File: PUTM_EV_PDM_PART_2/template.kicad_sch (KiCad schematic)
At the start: 4 parts, among them J1 CONN IN, J3 Conn_02x18_Counter_Clockwise, J4 WIRE OUT, J5 Conn_01x37

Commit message: Add files via upload
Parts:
- removed J4: WIRE OUT, Connector_Wire:SolderWire-0.75sqmm_1x02_P4.8mm_D1.25mm_OD2.3mm_Relief, symbol Connector:Conn_01x02_Pin
- removed J5: Conn_01x37, 3RD_party:37 PIN DEUTSCH, symbol Connector_Generic:Conn_01x37
- added J2, J7: UPS-08-07.0-01-L-V, UPS0807001LV, symbol UPS-08-07.0-01-L-V:UPS-08-07.0-01-L-V
- added J4: Conn_01x06_Pin, Connector_IDC:IDC-Header_2x03_P2.54mm_Vertical, symbol Connector:Conn_01x06_Pin
- added J6: +24V OUT, UPT-02-01-01-L-V:SAMTEC_UPT-02-03.0-XX-X-V, symbol Connector:Conn_01x02_Pin
- J1: value CONN IN -> +24V IN; footprint (none) -> DPT13-4P:TE_DTP13-4P
- J3: footprint Connector_IDC:IDC-Header_2x20-1MP_P2.54mm_Latch6.5mm_Vertical -> 3RD_party:37 PIN DEUTSCH
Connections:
- net DASH 24VDC is gone; now on net BRAKE BALANCE 24VDC: J3.15 (Pin_15)
- net DIAGPORT 24VDC is gone; now on net AIR PRESSURE 24VDC: J3.21 (Pin_21)
- net FRONT BOX 24VDC is gone; now on net BRAKE BALANCE 24VDC: J3.28 (Pin_28)
- net HV LOGIKA 2 24VDC is gone; now on net HV LOGIKA 1 24VDC: J3.33 (Pin_33)
- net INVERTER 2 24VDC is gone; now on net INVERTER 1 24VDC: J3.30 (Pin_30)
- net IR CAMS FRONT 24VDC is gone; now on net AIR PRESSURE 24VDC: J3.6 (Pin_6)
- net IR CAMS REAR 24VDC is gone; now on net AIR PRESSURE 24VDC: J3.22 (Pin_22)
- net ODRIVE 3 24VDC is gone; now on net ODRIVE 2 24VDC: J3.24 (Pin_24)
- net ODRIVE 5 24VDC is gone; now on net ODRIVE 4 24VDC: J3.26 (Pin_26)
- net PC 24VDC 2 is gone; now on net PC 24VDC 1: J3.27 (Pin_27)
- net PC 24VDC 4 is gone; now on net PC 24VDC 3: J3.17 (Pin_17)
- net REARBOX 2 24VDC is gone; now on net REARBOX 1 24VDC: J3.3 (Pin_3)
- net REARBOX 4 24VDC is gone; now on net REARBOX 3 24VDC: J3.8 (Pin_8)
- net SDC SOURCE is gone; now on net ASMS SOURCE: J3.9 (Pin_9)
- net TSAL LIGHT 24VDC is gone; now on net BSPD 24VDC: J3.20 (Pin_20)
- net TSAL LOGIC 24VDC is gone; now on net BSPD 24VDC: J3.19 (Pin_19)
- net +24V: now also J6.1 (Pin_1)
- net AIR PRESSURE 24VDC: now also J7.D1, J7.D2, J7.D3, J7.D4, J7.D5, J7.D6
- net ASMS IN: now also J4.3 (Pin_3)
- net ASMS SOURCE: now also J2.C1, J2.C2, J2.C3, J2.C4, J2.C5, J2.C6
- net BRAKE BALANCE 24VDC: now also J2.F1, J2.F2, J2.F3, J2.F4, J2.F5, J2.F6
- net BSPD 24VDC: now also J7.H1, J7.H2, J7.H3, J7.H4, J7.H5, J7.H6
- net CAN_H: now also J4.2 (Pin_2)
- net CAN_L: now also J4.1 (Pin_1)
- net GND: now also J6.2 (Pin_2)
- net GND PDM: now also J4.4 (Pin_4), J4.5 (Pin_5), J4.6 (Pin_6), J7.A1, J7.A2, J7.A3, J7.A4, J7.A5, J7.A6
- net HV LOGIKA 1 24VDC: now also J2.A1, J2.A2, J2.A3, J2.A4, J2.A5, J2.A6
- net INVERTER 1 24VDC: now also J2.G1, J2.G2, J2.G3, J2.G4, J2.G5, J2.G6
- net ODRIVE 1 24VDC: now also J2.D1, J2.D2, J2.D3, J2.D4, J2.D5, J2.D6
- net ODRIVE 2 24VDC: now also J7.F1, J7.F2, J7.F3, J7.F4, J7.F5, J7.F6
- net ODRIVE 4 24VDC: now also J2.B1, J2.B2, J2.B3, J2.B4, J2.B5, J2.B6
- net PC 24VDC 1: now also J2.E1, J2.E2, J2.E3, J2.E4, J2.E5, J2.E6
- net PC 24VDC 3: now also J2.H1, J2.H2, J2.H3, J2.H4, J2.H5, J2.H6
- net PC 24VDC 5: now also J7.G1, J7.G2, J7.G3, J7.G4, J7.G5, J7.G6
- net REARBOX 1 24VDC: now also J7.B1, J7.B2, J7.B3, J7.B4, J7.B5, J7.B6
- net REARBOX 3 24VDC: now also J7.E1, J7.E2, J7.E3, J7.E4, J7.E5, J7.E6
- net REARBOX 5 24VDC: now also J7.C1, J7.C2, J7.C3, J7.C4, J7.C5, J7.C6

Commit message: Add files via upload
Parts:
- removed J1: +24V IN, DPT13-4P:TE_DTP13-4P, symbol Connector:Conn_01x02_Pin
- removed J4: Conn_01x06_Pin, Connector_IDC:IDC-Header_2x03_P2.54mm_Vertical, symbol Connector:Conn_01x06_Pin
- removed J6: +24V OUT, UPT-02-01-01-L-V:SAMTEC_UPT-02-03.0-XX-X-V, symbol Connector:Conn_01x02_Pin
- added J4: Conn_01x06, Connector_IDC:IDC-Header_2x03_P2.54mm_Vertical, symbol Connector_Generic:Conn_01x06
- added J5: +24V OUT, UPT-02-01-01-L-V:SAMTEC_UPT-02-03.0-XX-X-V, symbol Connector_Generic:Conn_01x02
- added J8: +24V IN, DPT13-4P:TE_DTP13-4P, symbol Connector_Generic:Conn_01x02
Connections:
- net +24V: now also J5.1 (Pin_1), J8.1 (Pin_1)
- net ASMS IN: now also J4.3 (Pin_3)
- net CAN_H: now also J4.2 (Pin_2)
- net CAN_L: now also J4.1 (Pin_1)
- net GND: now also J5.2 (Pin_2), J8.2 (Pin_2)
- net GND PDM: now also J4.4 (Pin_4), J4.5 (Pin_5), J4.6 (Pin_6)
- net INVERTER 1 24VDC: now also J2.H1, J2.H2, J2.H3, J2.H4, J2.H5, J2.H6; no longer J2.G1, J2.G2, J2.G3, J2.G4, J2.G5, J2.G6
- net ODRIVE 2 24VDC: now also J7.G1, J7.G2, J7.G3, J7.G4, J7.G5, J7.G6; no longer J7.F1, J7.F2, J7.F3, J7.F4, J7.F5, J7.F6
- net PC 24VDC 3: now also J2.G1, J2.G2, J2.G3, J2.G4, J2.G5, J2.G6; no longer J2.H1, J2.H2, J2.H3, J2.H4, J2.H5, J2.H6
- net PC 24VDC 5: now also J7.F1, J7.F2, J7.F3, J7.F4, J7.F5, J7.F6; no longer J7.G1, J7.G2, J7.G3, J7.G4, J7.G5, J7.G6

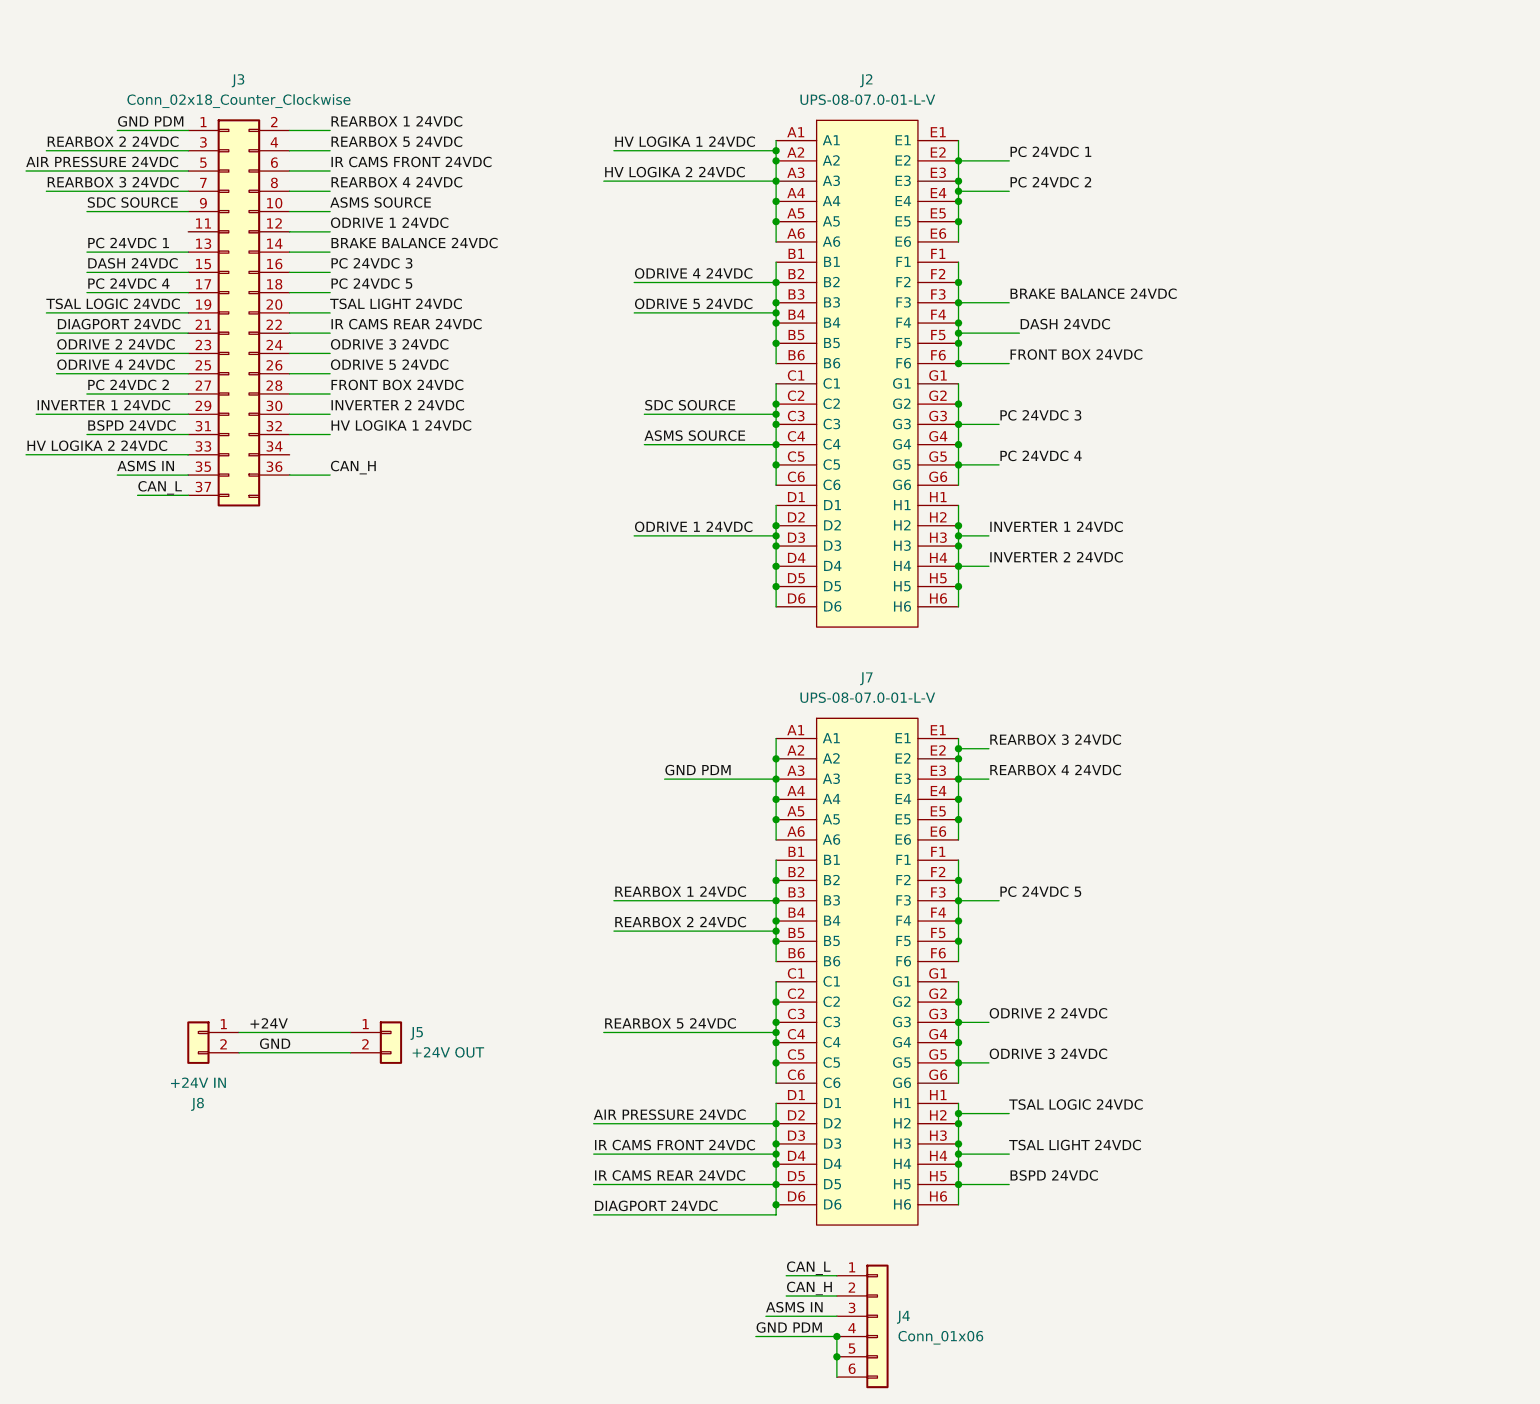
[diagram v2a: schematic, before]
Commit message: Removed ODRIVE
+fixed copper plates
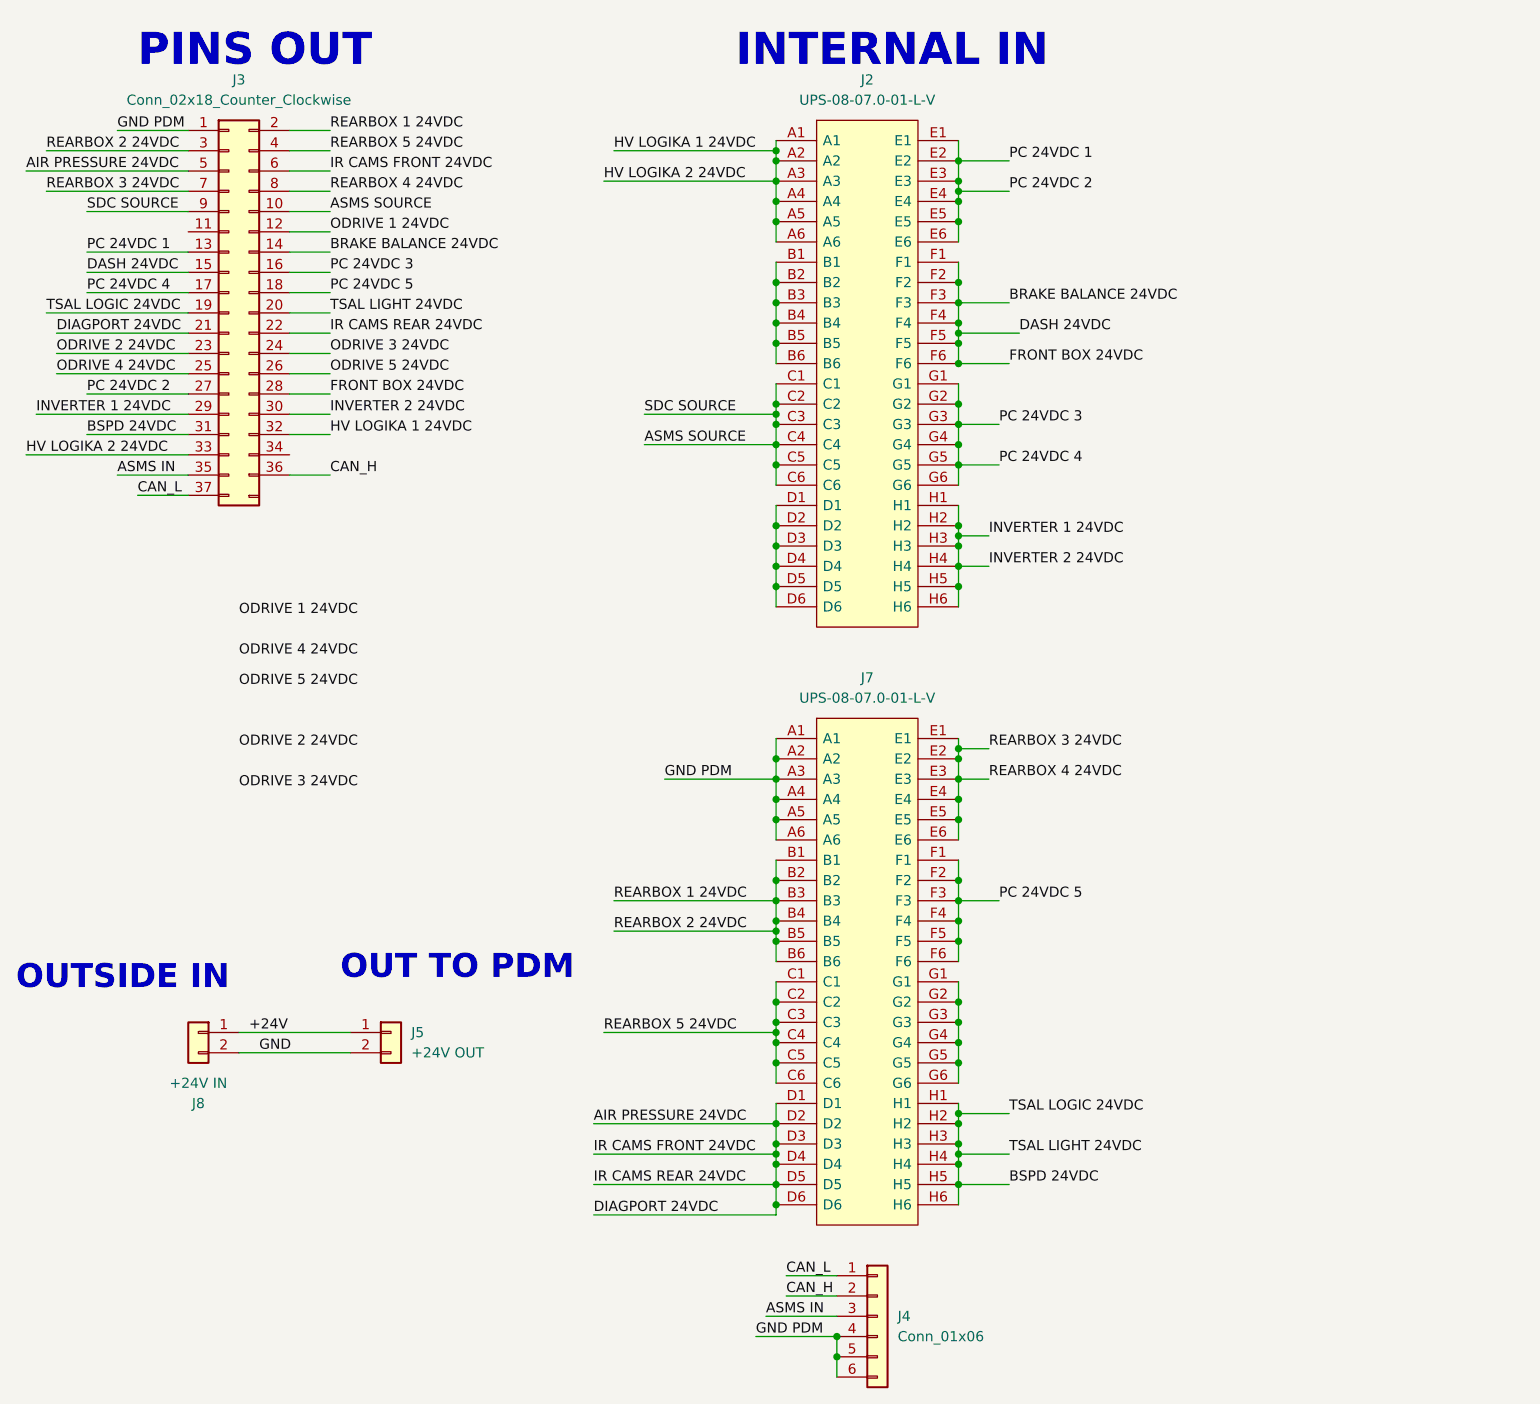
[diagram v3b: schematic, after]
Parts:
- J5: footprint UPT-02-01-01-L-V:SAMTEC_UPT-02-03.0-XX-X-V -> UPS-02-04.0-01-L-V:SAMTEC_UPS-02-04.0-01-L-V
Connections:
- net ODRIVE 1 24VDC: no longer J2.D1, J2.D2, J2.D3, J2.D4, J2.D5, J2.D6
- net ODRIVE 2 24VDC: no longer J3.24 (Pin_24), J7.G1, J7.G2, J7.G3, J7.G4, J7.G5, J7.G6
- net ODRIVE 4 24VDC: no longer J2.B1, J2.B2, J2.B3, J2.B4, J2.B5, J2.B6, J3.26 (Pin_26)
- new net: J7.G1, J7.G2, J7.G3, J7.G4, J7.G5, J7.G6
- new net: J2.B1, J2.B2, J2.B3, J2.B4, J2.B5, J2.B6
- new net: J2.D1, J2.D2, J2.D3, J2.D4, J2.D5, J2.D6
- new net ODRIVE 3 24VDC: J3.24 (Pin_24)
- new net ODRIVE 5 24VDC: J3.26 (Pin_26)
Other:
- note added: "INTERNAL IN"
- note added: "OUT TO PDM"
- note added: "OUTSIDE IN"
- note added: "PINS OUT"
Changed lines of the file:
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@@
   (junction (at 133.35 81.28) (diameter 0) (color 0 0 0 0)
   )
-  (junction (at 110.49 77.47) (diameter 0) (color 0 0 0 0)
-  )
   (junction (at 133.35 105.41) (diameter 0) (color 0 0 0 0)
   )
@@
   (junction (at 133.35 76.2) (diameter 0) (color 0 0 0 0)
   )
-  (junction (at 110.49 49.53) (diameter 0) (color 0 0 0 0)
-  )
-  (wire (pts (xy 92.71 77.47) (xy 110.49 77.47))
-    (stroke (width 0) (type default))
-  )
   (wire (pts (xy 24.13 59.69) (xy 36.83 59.69))
     (stroke (width 0) (type default))
@@
     (stroke (width 0) (type default))
   )
-  (wire (pts (xy 110.49 77.47) (xy 110.49 78.74))
+  (wire (pts (xy 110.49 76.2) (xy 110.49 78.74))
     (stroke (width 0) (type default))
   )
@@
     (stroke (width 0) (type default))
   )
-  (wire (pts (xy 133.35 138.43) (xy 137.16 138.43))
-    (stroke (width 0) (type default))
-  )
   (wire (pts (xy 110.49 66.04) (xy 110.49 68.58))
     (stroke (width 0) (type default))
@@
     (stroke (width 0) (type default))
   )
-  (wire (pts (xy 92.71 45.72) (xy 110.49 45.72))
-    (stroke (width 0) (type default))
-  )
   (wire (pts (xy 87.63 151.13) (xy 110.49 151.13))
     (stroke (width 0) (type default))
@@
     (stroke (width 0) (type default))
   )
-  (wire (pts (xy 110.49 48.26) (xy 110.49 49.53))
+  (wire (pts (xy 110.49 48.26) (xy 110.49 50.8))
     (stroke (width 0) (type default))
   )
@@
     (stroke (width 0) (type default))
   )
-  (wire (pts (xy 92.71 49.53) (xy 110.49 49.53))
-    (stroke (width 0) (type default))
-  )
   (wire (pts (xy 107.95 177.8) (xy 118.11 177.8))
     (stroke (width 0) (type default))
@@
     (stroke (width 0) (type default))
   )
-  (wire (pts (xy 133.35 143.51) (xy 137.16 143.51))
-    (stroke (width 0) (type default))
-  )
-  (wire (pts (xy 110.49 49.53) (xy 110.49 50.8))
-    (stroke (width 0) (type default))
-  )
   (wire (pts (xy 110.49 128.27) (xy 110.49 130.81))
     (stroke (width 0) (type default))
@@
     (stroke (width 0) (type default))
   )
-  (wire (pts (xy 110.49 76.2) (xy 110.49 77.47))
-    (stroke (width 0) (type default))
-  )
   (wire (pts (xy 20.32 52.07) (xy 36.83 52.07))
     (stroke (width 0) (type default))
@@
     (stroke (width 0) (type default))
   )
+  (text "INTERNAL IN" (at 105.41 19.05 0)
+    (effects (font (size 4 4) bold) (justify left bottom))
+  )
+  (text "OUTSIDE IN " (at 15.24 134.62 0)
+    (effects (font (size 3 3) bold) (justify left bottom))
+  )
+  (text "OUT TO PDM" (at 55.88 133.35 0)
+    (effects (font (size 3 3) bold) (justify left bottom))
+  )
+  (text "PINS OUT\n" (at 30.48 19.05 0)
+    (effects (font (size 4 4) (thickness 0.8) bold) (justify left bottom))
+  )
   (label "PC 24VDC 4" (at 24.13 46.99 0) (fields_autoplaced)
     (effects (font (size 1.27 1.27)) (justify left bottom))
@@
     (effects (font (size 1.27 1.27)) (justify left bottom))
   )
-  (label "ODRIVE 3 24VDC" (at 137.16 143.51 0) (fields_autoplaced)
+  (label "ODRIVE 3 24VDC" (at 43.18 109.22 0) (fields_autoplaced)
     (effects (font (size 1.27 1.27)) (justify left bottom))
   )
@@
     (effects (font (size 1.27 1.27)) (justify left bottom))
   )
-  (label "ODRIVE 5 24VDC" (at 92.71 49.53 0) (fields_autoplaced)
+  (label "ODRIVE 5 24VDC" (at 43.18 96.52 0) (fields_autoplaced)
     (effects (font (size 1.27 1.27)) (justify left bottom))
   )
@@
     (effects (font (size 1.27 1.27)) (justify left bottom))
   )
-  (label "ODRIVE 4 24VDC" (at 92.71 45.72 0) (fields_autoplaced)
+  (label "ODRIVE 4 24VDC" (at 43.18 92.71 0) (fields_autoplaced)
     (effects (font (size 1.27 1.27)) (justify left bottom))
   )
@@
     (effects (font (size 1.27 1.27)) (justify left bottom))
   )
-  (label "ODRIVE 1 24VDC" (at 92.71 77.47 0) (fields_autoplaced)
+  (label "ODRIVE 1 24VDC" (at 43.18 87.63 0) (fields_autoplaced)
     (effects (font (size 1.27 1.27)) (justify left bottom))
   )
@@
     (effects (font (size 1.27 1.27)) (justify left bottom))
   )
-  (label "ODRIVE 2 24VDC" (at 137.16 138.43 0) (fields_autoplaced)
+  (label "ODRIVE 2 24VDC" (at 43.18 104.14 0) (fields_autoplaced)
     (effects (font (size 1.27 1.27)) (justify left bottom))
   )
@@
       (effects (font (size 1.27 1.27)) (justify left))
     )
-    (property "Footprint" "UPT-02-01-01-L-V:SAMTEC_UPT-02-03.0-XX-X-V" (at 62.23 139.7 0)
+    (property "Footprint" "UPS-02-04.0-01-L-V:SAMTEC_UPS-02-04.0-01-L-V" (at 62.23 139.7 0)
       (effects (font (size 1.27 1.27)) hide)
     )
